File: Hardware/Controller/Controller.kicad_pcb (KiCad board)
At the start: 2 copper layers, 20.3 x 80.8 mm, 5 parts, among them J101 Conn_01x04, SW101 DAY_RESET, SW102 DAY_ADV, SW103 DAY_SUB

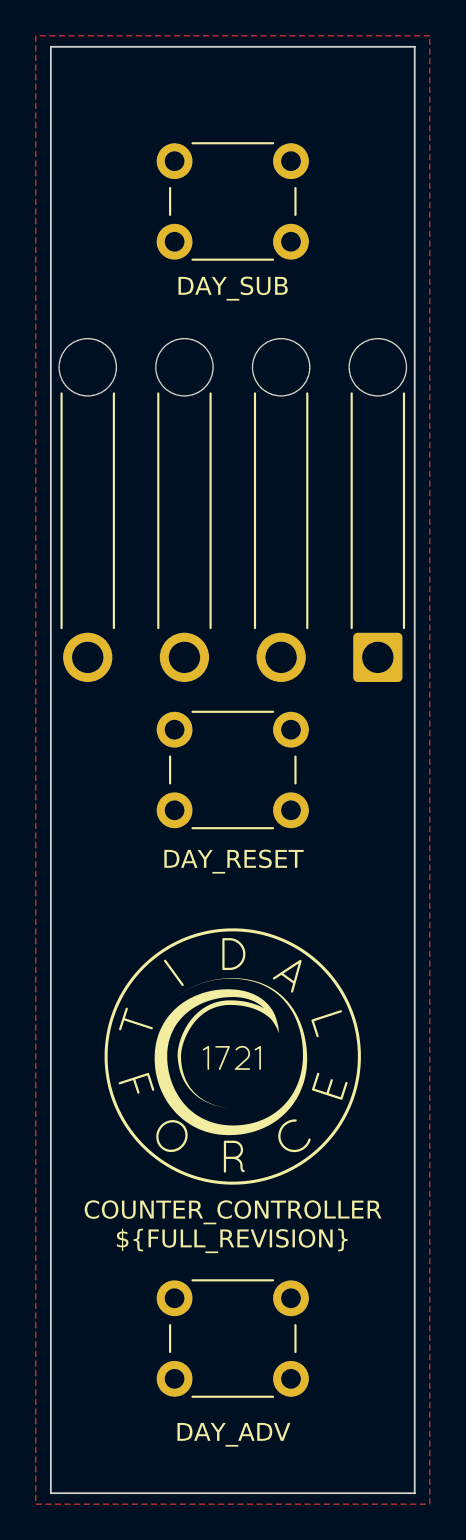
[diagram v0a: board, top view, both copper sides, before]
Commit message: Add routes
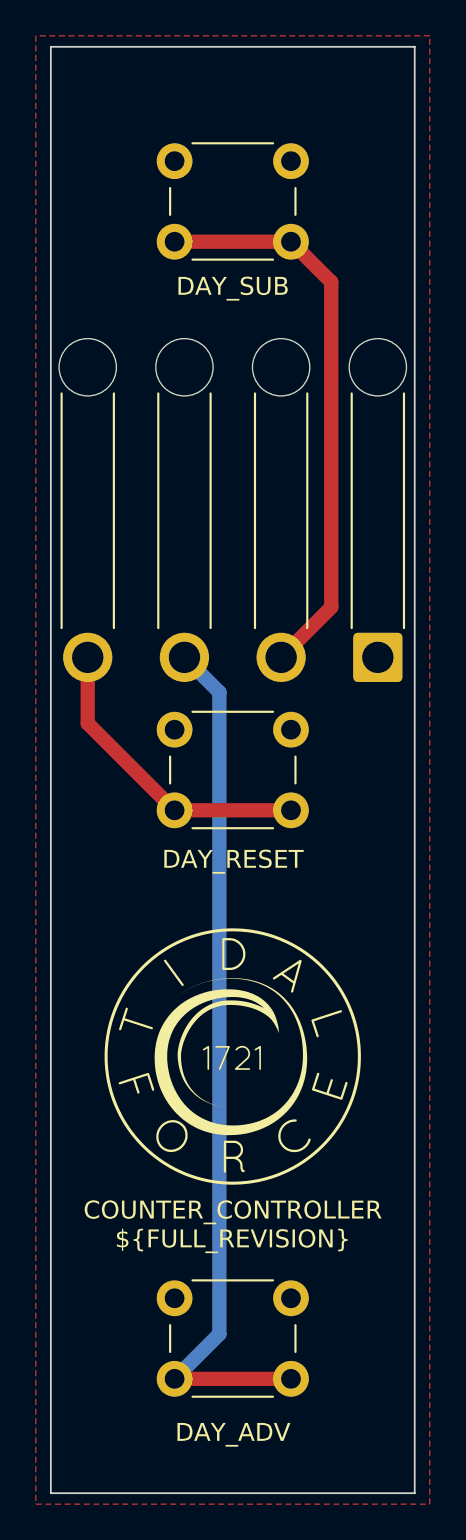
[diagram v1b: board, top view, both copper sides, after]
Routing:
- net Net-(J101-Pin_3): track 0.00 -> 48.6 mm
- net Net-(J101-Pin_2): track 0.00 -> 31.8 mm
- net Net-(J101-Pin_4): track 0.00 -> 17.0 mm
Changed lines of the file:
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@@
     (effects (font (size 1 1) (thickness 0.15)) (justify top))
   )
+  (segment (start 5.5 -9.09) (end 2.7 -6.29) (width 0.8) (layer "F.Cu") (net 2))
+  (segment (start 3.25 -29.5) (end 5.5 -27.25) (width 0.8) (layer "F.Cu") (net 2))
+  (segment (start 5.5 -27.25) (end 5.5 -9.09) (width 0.8) (layer "F.Cu") (net 2))
+  (segment (start -3.25 -29.5) (end 3.25 -29.5) (width 0.8) (layer "F.Cu") (net 2))
+  (segment (start -3.25 34) (end 3.25 34) (width 0.8) (layer "F.Cu") (net 3))
+  (segment (start -3.25 34) (end -0.75 31.5) (width 0.8) (layer "B.Cu") (net 3))
+  (segment (start -0.75 -4.34) (end -2.7 -6.29) (width 0.8) (layer "B.Cu") (net 3))
+  (segment (start -0.75 31.5) (end -0.75 -4.34) (width 0.8) (layer "B.Cu") (net 3))
+  (segment (start -8.1 -2.6) (end -8.1 -6.29) (width 0.8) (layer "F.Cu") (net 4))
+  (segment (start -3.25 2.25) (end -8.1 -2.6) (width 0.8) (layer "F.Cu") (net 4))
+  (segment (start -3.25 2.25) (end 3.25 2.25) (width 0.8) (layer "F.Cu") (net 4))
   (zone (net 1) (net_name "+5V") (layer "F.Cu") (hatch edge 0.5)
     (connect_pads (clearance 0.5))
